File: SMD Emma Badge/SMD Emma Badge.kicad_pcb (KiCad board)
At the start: 2 copper layers, 1 part, among them J1 Conn_01x02_Male

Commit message: Working through basics of the LFSR
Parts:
- added C201: 10u, Capacitor_SMD:C_0603_1608Metric, F.Cu at (146.1, 80.0)
- added C202: 8.2n, Capacitor_SMD:C_0603_1608Metric, F.Cu at (158.8, 78.7)
- added C203: 0.1uF, Capacitor_SMD:C_0603_1608Metric, F.Cu at (157.5, 71.1)
- added C301: 10u, Capacitor_SMD:C_0603_1608Metric, F.Cu at (82.5, 74.9)
- added C302: 8.2n, Capacitor_SMD:C_0603_1608Metric, F.Cu at (96.1, 72.4)
- added C303: 0.1uF, Capacitor_SMD:C_0603_1608Metric, F.Cu at (96.5, 68.6)
- added C401: 0.1uF, Capacitor_SMD:C_0603_1608Metric, F.Cu at (96.5, 88.9)
- added C402: 0.1uF, Capacitor_SMD:C_0603_1608Metric, F.Cu at (97.8, 77.5)
- added C403: 0.1uF, Capacitor_SMD:C_0603_1608Metric, F.Cu at (110.5, 87.6)
- added C404: 0.1uF, Capacitor_SMD:C_0603_1608Metric, F.Cu at (127.0, 87.6)
- added C405: 0.1uF, Capacitor_SMD:C_0603_1608Metric, F.Cu at (113.0, 77.5)
- added R201: 11k, Resistor_SMD:R_0603_1608Metric, F.Cu at (146.1, 72.4)
- added R202: 11k, Resistor_SMD:R_0603_1608Metric, F.Cu at (146.1, 76.2)
- added R203: 1k, Resistor_SMD:R_0603_1608Metric, F.Cu at (162.6, 73.7)
- added R301: 1k, Resistor_SMD:R_0603_1608Metric, F.Cu at (82.5, 67.3)
- added R302: 1k, Resistor_SMD:R_0603_1608Metric, F.Cu at (82.5, 71.1)
- added R303: 1k, Resistor_SMD:R_0603_1608Metric, F.Cu at (101.6, 68.6)
- added U101: AMS1117-5.0, Package_TO_SOT_SMD:SOT-223-3_TabPin2, F.Cu at (127.0, 67.3)
- added U201: LM555xM, Package_SO:SOIC-8_3.9x4.9mm_P1.27mm, F.Cu at (152.8, 76.8)
- added U301: LM555xM, Package_SO:SOIC-8_3.9x4.9mm_P1.27mm, F.Cu at (89.8, 70.7)
- added U401: 74164, Package_SO:SOIC-14_3.9x8.7mm_P1.27mm, F.Cu at (102.9, 92.7)
- added U402: 74LS595, Package_SO:SOIC-16_3.9x9.9mm_P1.27mm, F.Cu at (118.1, 92.7)
- added U403: 74164, Package_SO:SOIC-14_3.9x8.7mm_P1.27mm, F.Cu at (133.3, 92.7)
- added U404: 74HC86, Package_SO:SOIC-14_3.9x8.7mm_P1.27mm, F.Cu at (118.1, 83.8)
- added U405: 74HC04, Package_SO:SOIC-14_3.9x8.7mm_P1.27mm, F.Cu at (102.9, 83.8)
- renumbered J1 to J101
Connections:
- J101 pad 2: Net-(J1-Pad2) -> GND

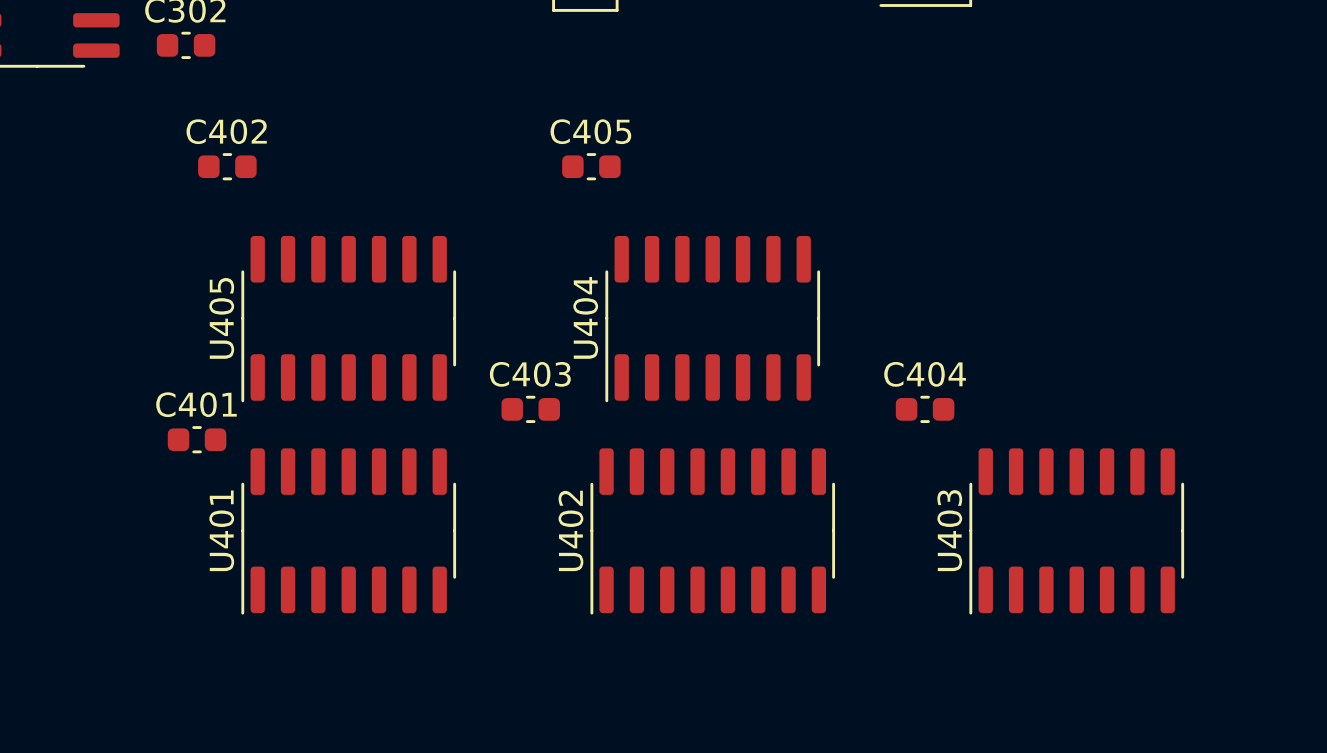
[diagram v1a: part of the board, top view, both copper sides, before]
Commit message: Add power-on reset
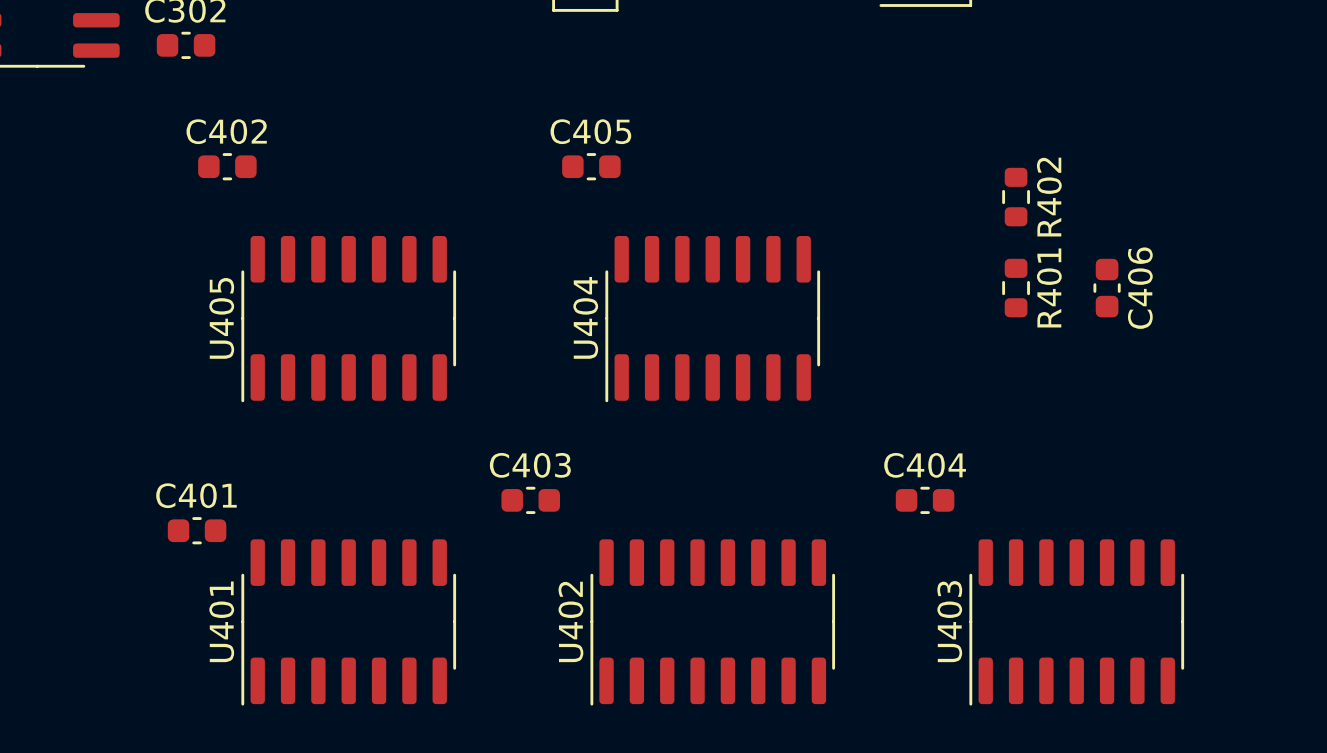
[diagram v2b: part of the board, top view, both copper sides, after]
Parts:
- added C406: 10u, Capacitor_SMD:C_0603_1608Metric, F.Cu at (134.6, 82.5)
- added R401: 180k, Resistor_SMD:R_0603_1608Metric, F.Cu at (130.8, 82.5)
- added R402: 1k, Resistor_SMD:R_0603_1608Metric, F.Cu at (130.8, 78.7)
- moved C403 3.81 mm to (110.5, 91.4)
- moved C404 3.81 mm to (127.0, 91.4)
- moved U401 3.81 mm to (102.9, 96.5)
- moved U402 3.81 mm to (118.1, 96.5)
- moved U403 3.81 mm to (133.3, 96.5)
- moved C401 3.81 mm to (96.5, 92.7)

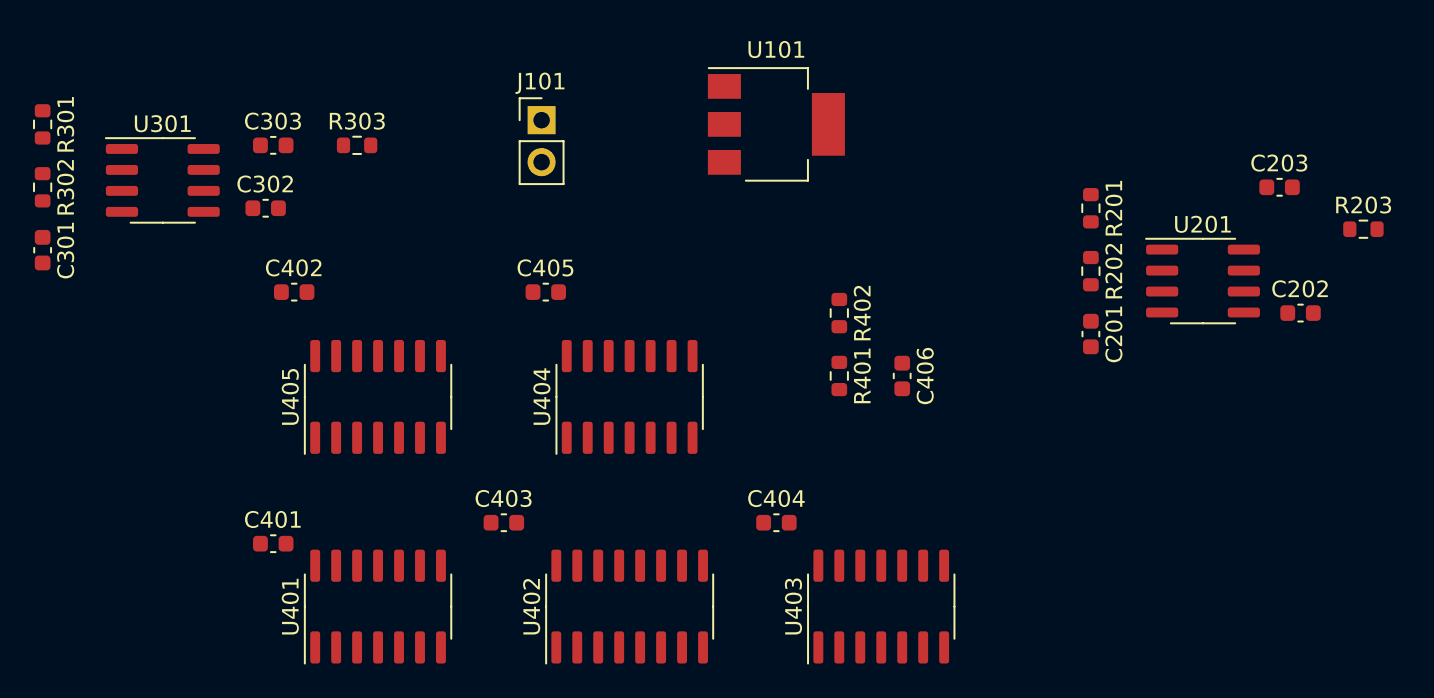
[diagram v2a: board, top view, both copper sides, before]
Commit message: Routing the registers
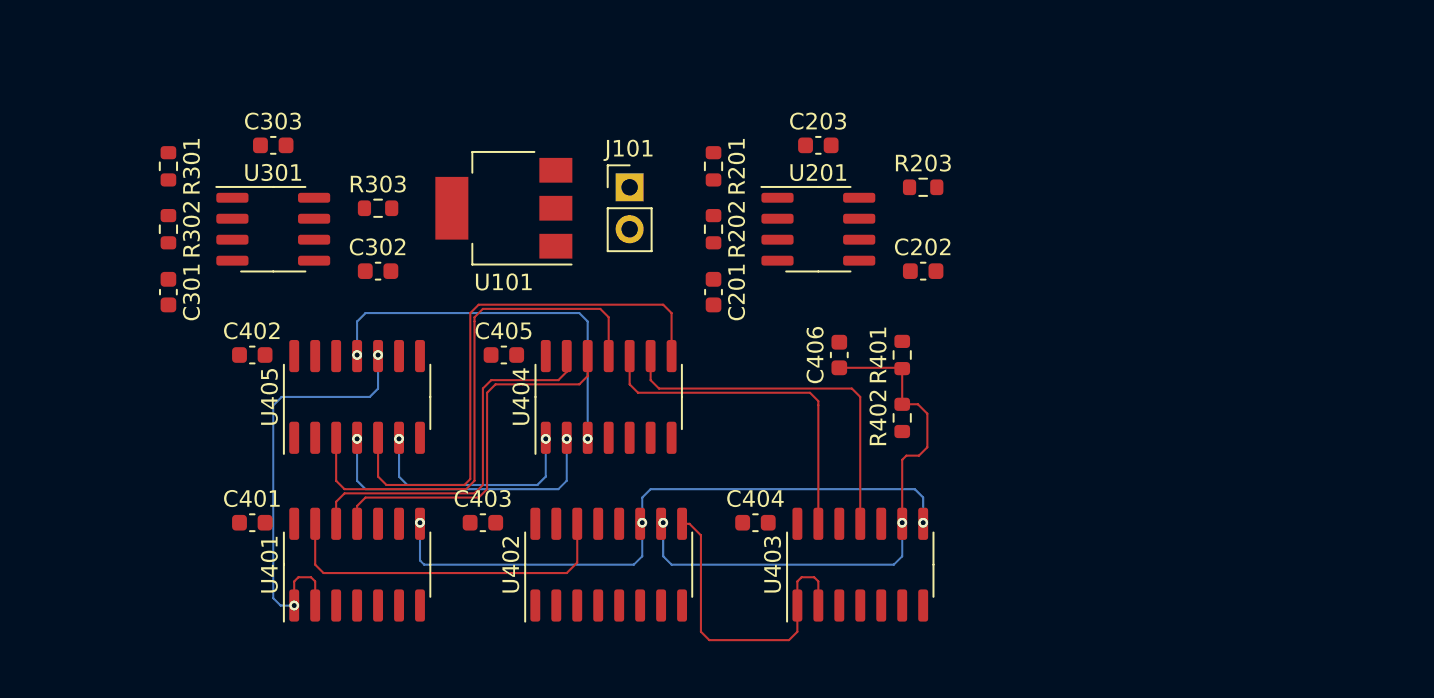
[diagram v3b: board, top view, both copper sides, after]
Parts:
- moved C203 28.1 mm to (129.5, 68.6)
- moved R203 26.8 mm to (135.9, 71.1)
- moved U201 23.5 mm to (129.5, 73.7)
- moved C201 23.0 mm to (123.2, 77.5)
- moved C202 23.0 mm to (135.9, 76.2)
- moved R201 23.0 mm to (123.2, 69.8)
- moved R202 23.0 mm to (123.2, 73.7)
- moved U101 17.3 mm to (110.5, 72.4), turned to 180 degrees
- moved C301 8.03 mm to (90.2, 77.5)
- moved R301 8.03 mm to (90.2, 69.8)
- moved R302 8.03 mm to (90.2, 73.7)
- moved C302 7.80 mm to (102.9, 76.2)
- moved R402 7.41 mm to (134.6, 85.1), turned to 90 degrees
- moved U301 7.31 mm to (96.5, 73.7)
- moved J101 6.71 mm to (118.1, 71.1)
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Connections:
- C203 pad 1: +5V -> GND
- C203 pad 2: GND -> +5V
- C303 pad 1: +5V -> GND
- C303 pad 2: GND -> +5V
- C401 pad 1: +5V -> GND
- C401 pad 2: GND -> +5V
- C404 pad 1: +5V -> GND
- C404 pad 2: GND -> +5V
- U404 pad 1: /LFSR/TAP6 -> Net-(U404-Pad1)
- U404 pad 10: Net-(U404-Pad10) -> /LFSR/TAP24
- U404 pad 12: GND -> /LFSR/TAP6
- U404 pad 13: GND -> /LFSR/TAP7
- U404 pad 2: /LFSR/TAP7 -> Net-(U404-Pad2)
- U404 pad 4: /LFSR/TAP22 -> GND
- U404 pad 5: /LFSR/TAP24 -> GND
- U404 pad 9: Net-(U404-Pad9) -> /LFSR/TAP22
- U405 pad 1: Net-(U404-Pad3) -> GND
- U405 pad 10: Net-(U405-Pad10) -> /LFSR/INPUT
- U405 pad 11: GND -> Net-(U404-Pad3)
- U405 pad 2: Net-(U404-Pad9) -> Net-(U405-Pad2)
- U405 pad 3: Net-(U404-Pad6) -> Net-(U404-Pad11)
- U405 pad 4: Net-(U404-Pad10) -> Net-(U404-Pad2)
- U405 pad 6: /LFSR/INPUT -> Net-(U404-Pad1)
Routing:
- net /Register Clock/CLK: track 0.00 -> 38.6 mm, vias 0 -> 3
- net /LFSR/PWRCLR: track 0.00 -> 34.5 mm, vias 0 -> 2
- net Net-(U404-Pad8): track 0.00 -> 33.6 mm
- net Net-(U404-Pad11): track 0.00 -> 32.2 mm
- net /LFSR/INPUT: track 0.00 -> 26.3 mm, vias 0 -> 2
- net Net-(U404-Pad3): track 0.00 -> 23.5 mm, vias 0 -> 2
- net /LFSR/TAP7: track 0.00 -> 22.9 mm
- net /LFSR/TAP6: track 0.00 -> 22.9 mm
- net /LFSR/TAP22: track 0.00 -> 22.3 mm
- net Net-(U401-Pad13): track 0.00 -> 21.2 mm
- net /LFSR/TAP24: track 0.00 -> 21.0 mm
- net Net-(U402-Pad9): track 0.00 -> 19.5 mm
- net Net-(U404-Pad2): track 0.00 -> 18.2 mm, vias 0 -> 2
- net Net-(U404-Pad1): track 0.00 -> 13.9 mm, vias 0 -> 2

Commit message: Working on letters
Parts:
- added D501: LED, LED_SMD:LED_0603_1608Metric, F.Cu at (69.8, 108.0)
- added D502: LED, LED_SMD:LED_0603_1608Metric, F.Cu at (73.7, 108.0)
- added D503: LED, LED_SMD:LED_0603_1608Metric, F.Cu at (77.5, 108.0)
- added D504: LED, LED_SMD:LED_0603_1608Metric, F.Cu at (81.3, 108.0)
- added D505: LED, LED_SMD:LED_0603_1608Metric, F.Cu at (85.1, 108.0)
- added D506: LED, LED_SMD:LED_0603_1608Metric, F.Cu at (69.8, 111.5)
- added D507: LED, LED_SMD:LED_0603_1608Metric, F.Cu at (69.8, 115.1)
- added D508: LED, LED_SMD:LED_0603_1608Metric, F.Cu at (69.8, 118.6)
- added D509: LED, LED_SMD:LED_0603_1608Metric, F.Cu at (73.7, 118.6)
- added D510: LED, LED_SMD:LED_0603_1608Metric, F.Cu at (77.5, 118.6)
- added D511: LED, LED_SMD:LED_0603_1608Metric, F.Cu at (81.3, 118.6)
- added D512: LED, LED_SMD:LED_0603_1608Metric, F.Cu at (69.8, 122.2)
- added D513: LED, LED_SMD:LED_0603_1608Metric, F.Cu at (69.8, 125.7)
- added D514: LED, LED_SMD:LED_0603_1608Metric, F.Cu at (69.8, 129.3)
- added D515: LED, LED_SMD:LED_0603_1608Metric, F.Cu at (73.7, 129.3)
- added D516: LED, LED_SMD:LED_0603_1608Metric, F.Cu at (77.5, 129.3)
- added D517: LED, LED_SMD:LED_0603_1608Metric, F.Cu at (81.3, 129.3)
- added D518: LED, LED_SMD:LED_0603_1608Metric, F.Cu at (85.1, 129.3)
- added D601: LED, LED_SMD:LED_0603_1608Metric, F.Cu at (91.4, 108.0)
- added D602: LED, LED_SMD:LED_0603_1608Metric, F.Cu at (106.7, 108.0)
- added D603: LED, LED_SMD:LED_0603_1608Metric, F.Cu at (91.4, 111.5)
- added D604: LED, LED_SMD:LED_0603_1608Metric, F.Cu at (95.2, 111.5)
- added D605: LED, LED_SMD:LED_0603_1608Metric, F.Cu at (102.9, 111.5)
- added D606: LED, LED_SMD:LED_0603_1608Metric, F.Cu at (106.7, 111.5)
- added D607: LED, LED_SMD:LED_0603_1608Metric, F.Cu at (91.4, 115.1)
- added D608: LED, LED_SMD:LED_0603_1608Metric, F.Cu at (99.1, 115.1)
- added D609: LED, LED_SMD:LED_0603_1608Metric, F.Cu at (106.7, 115.1)
- added D610: LED, LED_SMD:LED_0603_1608Metric, F.Cu at (91.4, 118.6)
- added D611: LED, LED_SMD:LED_0603_1608Metric, F.Cu at (99.1, 118.6)
- added D612: LED, LED_SMD:LED_0603_1608Metric, F.Cu at (106.7, 118.6)
- added D613: LED, LED_SMD:LED_0603_1608Metric, F.Cu at (91.4, 122.2)
- added D614: LED, LED_SMD:LED_0603_1608Metric, F.Cu at (106.7, 122.2)
- added D615: LED, LED_SMD:LED_0603_1608Metric, F.Cu at (91.4, 125.7)
- added D616: LED, LED_SMD:LED_0603_1608Metric, F.Cu at (106.7, 125.7)
- added D617: LED, LED_SMD:LED_0603_1608Metric, F.Cu at (91.4, 129.3)
- added D618: LED, LED_SMD:LED_0603_1608Metric, F.Cu at (106.7, 129.3)
- added D701: LED, LED_SMD:LED_0603_1608Metric, F.Cu at (113.0, 108.0)
- added D702: LED, LED_SMD:LED_0603_1608Metric, F.Cu at (128.3, 108.0)
- added D703: LED, LED_SMD:LED_0603_1608Metric, F.Cu at (113.0, 111.5)
- added D704: LED, LED_SMD:LED_0603_1608Metric, F.Cu at (116.8, 111.5)
- added D705: LED, LED_SMD:LED_0603_1608Metric, F.Cu at (124.5, 111.5)
- added D706: LED, LED_SMD:LED_0603_1608Metric, F.Cu at (128.3, 111.5)
- added D707: LED, LED_SMD:LED_0603_1608Metric, F.Cu at (113.0, 115.1)
- added D708: LED, LED_SMD:LED_0603_1608Metric, F.Cu at (120.7, 115.1)
- added D709: LED, LED_SMD:LED_0603_1608Metric, F.Cu at (128.3, 115.1)
- added D710: LED, LED_SMD:LED_0603_1608Metric, F.Cu at (113.0, 118.6)
- added D711: LED, LED_SMD:LED_0603_1608Metric, F.Cu at (120.7, 118.6)
- added D712: LED, LED_SMD:LED_0603_1608Metric, F.Cu at (128.3, 118.6)
- added D713: LED, LED_SMD:LED_0603_1608Metric, F.Cu at (113.0, 122.2)
- added D714: LED, LED_SMD:LED_0603_1608Metric, F.Cu at (128.3, 122.2)
- added D715: LED, LED_SMD:LED_0603_1608Metric, F.Cu at (113.0, 125.7)
- added D716: LED, LED_SMD:LED_0603_1608Metric, F.Cu at (128.3, 125.7)
- added D717: LED, LED_SMD:LED_0603_1608Metric, F.Cu at (113.0, 129.3)
- added D718: LED, LED_SMD:LED_0603_1608Metric, F.Cu at (128.3, 129.3)
- added D801: LED, LED_SMD:LED_0603_1608Metric, F.Cu at (142.2, 108.0)
- added D802: LED, LED_SMD:LED_0603_1608Metric, F.Cu at (138.4, 111.5)
- added D803: LED, LED_SMD:LED_0603_1608Metric, F.Cu at (146.1, 111.5)
- added D804: LED, LED_SMD:LED_0603_1608Metric, F.Cu at (134.6, 115.1)
- added D805: LED, LED_SMD:LED_0603_1608Metric, F.Cu at (149.9, 115.1)
- added D806: LED, LED_SMD:LED_0603_1608Metric, F.Cu at (134.6, 118.6)
- added D807: LED, LED_SMD:LED_0603_1608Metric, F.Cu at (149.9, 118.6)
- added D808: LED, LED_SMD:LED_0603_1608Metric, F.Cu at (134.6, 122.2)
- added D809: LED, LED_SMD:LED_0603_1608Metric, F.Cu at (138.4, 122.2)
- added D810: LED, LED_SMD:LED_0603_1608Metric, F.Cu at (142.2, 122.2)
- added D811: LED, LED_SMD:LED_0603_1608Metric, F.Cu at (146.1, 122.2)
- added D812: LED, LED_SMD:LED_0603_1608Metric, F.Cu at (149.9, 122.2)
- added D813: LED, LED_SMD:LED_0603_1608Metric, F.Cu at (134.6, 125.7)
- added D814: LED, LED_SMD:LED_0603_1608Metric, F.Cu at (149.9, 125.7)
- added D815: LED, LED_SMD:LED_0603_1608Metric, F.Cu at (134.6, 129.3)
- added D816: LED, LED_SMD:LED_0603_1608Metric, F.Cu at (149.9, 129.3)
- added H101: MountingHole, MountingHole:MountingHole_2.5mm, F.Cu at (71.1, 77.5)
- added H102: MountingHole, MountingHole:MountingHole_2.5mm, F.Cu at (148.6, 77.5)
- added Q501: MMBT3904, Package_TO_SOT_SMD:SOT-23, F.Cu at (77.5, 105.4)
- added Q601: MMBT3904, Package_TO_SOT_SMD:SOT-23, F.Cu at (99.1, 105.4)
- added Q701: MMBT3904, Package_TO_SOT_SMD:SOT-23, F.Cu at (120.7, 105.4)
- added Q801: MMBT3904, Package_TO_SOT_SMD:SOT-23, F.Cu at (142.2, 105.4)
- added R501: 1k, Resistor_SMD:R_0603_1608Metric, F.Cu at (69.8, 109.7)
- added R502: 1k, Resistor_SMD:R_0603_1608Metric, F.Cu at (73.7, 109.7)
- added R503: 1k, Resistor_SMD:R_0603_1608Metric, F.Cu at (77.5, 109.7)
- added R504: 1k, Resistor_SMD:R_0603_1608Metric, F.Cu at (81.3, 109.7)
- added R505: 1k, Resistor_SMD:R_0603_1608Metric, F.Cu at (85.1, 109.7)
- added R506: 1k, Resistor_SMD:R_0603_1608Metric, F.Cu at (69.8, 113.3)
- added R507: 1k, Resistor_SMD:R_0603_1608Metric, F.Cu at (69.8, 116.8)
- added R508: 1k, Resistor_SMD:R_0603_1608Metric, F.Cu at (69.8, 120.4)
- added R509: 1k, Resistor_SMD:R_0603_1608Metric, F.Cu at (73.7, 120.4)
- added R510: 1k, Resistor_SMD:R_0603_1608Metric, F.Cu at (77.5, 120.4)
- added R511: 1k, Resistor_SMD:R_0603_1608Metric, F.Cu at (81.3, 120.4)
- added R512: 1k, Resistor_SMD:R_0603_1608Metric, F.Cu at (69.8, 124.0)
- added R513: 1k, Resistor_SMD:R_0603_1608Metric, F.Cu at (69.8, 127.5)
- added R514: 1k, Resistor_SMD:R_0603_1608Metric, F.Cu at (69.8, 131.1)
- added R515: 1k, Resistor_SMD:R_0603_1608Metric, F.Cu at (73.7, 131.1)
- added R516: 1k, Resistor_SMD:R_0603_1608Metric, F.Cu at (77.5, 131.1)
- added R517: 1k, Resistor_SMD:R_0603_1608Metric, F.Cu at (81.3, 131.1)
- added R518: 1k, Resistor_SMD:R_0603_1608Metric, F.Cu at (85.1, 131.1)
- added R519: 11k, Resistor_SMD:R_0603_1608Metric, F.Cu at (78.7, 101.6)
- added R601: 1k, Resistor_SMD:R_0603_1608Metric, F.Cu at (91.4, 109.7)
- added R602: 1k, Resistor_SMD:R_0603_1608Metric, F.Cu at (106.7, 109.7)
- added R603: 1k, Resistor_SMD:R_0603_1608Metric, F.Cu at (91.4, 113.3)
- added R604: 1k, Resistor_SMD:R_0603_1608Metric, F.Cu at (95.2, 113.3)
- added R605: 1k, Resistor_SMD:R_0603_1608Metric, F.Cu at (102.9, 113.3)
- added R606: 1k, Resistor_SMD:R_0603_1608Metric, F.Cu at (106.7, 113.3)
- added R607: 1k, Resistor_SMD:R_0603_1608Metric, F.Cu at (91.4, 116.8)
- added R608: 1k, Resistor_SMD:R_0603_1608Metric, F.Cu at (99.1, 116.8)
- added R609: 1k, Resistor_SMD:R_0603_1608Metric, F.Cu at (106.7, 116.8)
- added R610: 1k, Resistor_SMD:R_0603_1608Metric, F.Cu at (91.4, 120.4)
- added R611: 1k, Resistor_SMD:R_0603_1608Metric, F.Cu at (99.1, 120.4)
- added R612: 1k, Resistor_SMD:R_0603_1608Metric, F.Cu at (106.7, 120.4)
- added R613: 1k, Resistor_SMD:R_0603_1608Metric, F.Cu at (91.4, 124.0)
- added R614: 1k, Resistor_SMD:R_0603_1608Metric, F.Cu at (106.7, 124.0)
- added R615: 1k, Resistor_SMD:R_0603_1608Metric, F.Cu at (91.4, 127.5)
- added R616: 1k, Resistor_SMD:R_0603_1608Metric, F.Cu at (106.7, 127.5)
- added R617: 1k, Resistor_SMD:R_0603_1608Metric, F.Cu at (91.4, 131.1)
- added R618: 1k, Resistor_SMD:R_0603_1608Metric, F.Cu at (106.7, 131.1)
- added R619: 11k, Resistor_SMD:R_0603_1608Metric, F.Cu at (100.3, 101.6)
- added R701: 1k, Resistor_SMD:R_0603_1608Metric, F.Cu at (113.0, 109.7)
- added R702: 1k, Resistor_SMD:R_0603_1608Metric, F.Cu at (128.3, 109.7)
- added R703: 1k, Resistor_SMD:R_0603_1608Metric, F.Cu at (113.0, 113.3)
- added R704: 1k, Resistor_SMD:R_0603_1608Metric, F.Cu at (116.8, 113.3)
- added R705: 1k, Resistor_SMD:R_0603_1608Metric, F.Cu at (124.5, 113.3)
- added R706: 1k, Resistor_SMD:R_0603_1608Metric, F.Cu at (128.3, 113.3)
- added R707: 1k, Resistor_SMD:R_0603_1608Metric, F.Cu at (113.0, 116.8)
- added R708: 1k, Resistor_SMD:R_0603_1608Metric, F.Cu at (120.7, 116.8)
- added R709: 1k, Resistor_SMD:R_0603_1608Metric, F.Cu at (128.3, 116.8)
- added R710: 1k, Resistor_SMD:R_0603_1608Metric, F.Cu at (113.0, 120.4)
- added R711: 1k, Resistor_SMD:R_0603_1608Metric, F.Cu at (120.7, 120.4)
- added R712: 1k, Resistor_SMD:R_0603_1608Metric, F.Cu at (128.3, 120.4)
- added R713: 1k, Resistor_SMD:R_0603_1608Metric, F.Cu at (113.0, 124.0)
- added R714: 1k, Resistor_SMD:R_0603_1608Metric, F.Cu at (128.3, 124.0)
- added R715: 1k, Resistor_SMD:R_0603_1608Metric, F.Cu at (113.0, 127.5)
- added R716: 1k, Resistor_SMD:R_0603_1608Metric, F.Cu at (128.3, 127.5)
- added R717: 1k, Resistor_SMD:R_0603_1608Metric, F.Cu at (113.0, 131.1)
- added R718: 1k, Resistor_SMD:R_0603_1608Metric, F.Cu at (128.3, 131.1)
- added R719: 11k, Resistor_SMD:R_0603_1608Metric, F.Cu at (121.9, 101.6)
- added R801: 1k, Resistor_SMD:R_0603_1608Metric, F.Cu at (142.2, 109.7)
- added R802: 1k, Resistor_SMD:R_0603_1608Metric, F.Cu at (138.4, 113.3)
- added R803: 1k, Resistor_SMD:R_0603_1608Metric, F.Cu at (146.1, 113.3)
- added R804: 1k, Resistor_SMD:R_0603_1608Metric, F.Cu at (134.6, 116.8)
- added R805: 1k, Resistor_SMD:R_0603_1608Metric, F.Cu at (149.9, 116.8)
- added R806: 1k, Resistor_SMD:R_0603_1608Metric, F.Cu at (134.6, 120.4)
- added R807: 1k, Resistor_SMD:R_0603_1608Metric, F.Cu at (149.9, 120.4)
- added R808: 1k, Resistor_SMD:R_0603_1608Metric, F.Cu at (134.6, 124.0)
- added R809: 1k, Resistor_SMD:R_0603_1608Metric, F.Cu at (138.4, 124.0)
- added R810: 1k, Resistor_SMD:R_0603_1608Metric, F.Cu at (142.2, 124.0)
- added R811: 1k, Resistor_SMD:R_0603_1608Metric, F.Cu at (146.1, 124.0)
- added R812: 1k, Resistor_SMD:R_0603_1608Metric, F.Cu at (149.9, 124.0)
- added R813: 1k, Resistor_SMD:R_0603_1608Metric, F.Cu at (134.6, 127.5)
- added R814: 1k, Resistor_SMD:R_0603_1608Metric, F.Cu at (149.9, 127.5)
- added R815: 1k, Resistor_SMD:R_0603_1608Metric, F.Cu at (134.6, 131.1)
- added R816: 1k, Resistor_SMD:R_0603_1608Metric, F.Cu at (149.9, 131.1)
- added R819: 11k, Resistor_SMD:R_0603_1608Metric, F.Cu at (143.5, 101.6)
- moved J101 46.2 mm to (73.7, 83.8), turned to 90 degrees
- moved U101 40.0 mm to (74.9, 90.8), turned to 270 degrees
- moved C202 31.0 mm to (148.6, 95.2), turned to 0 degrees
- moved R202 31.0 mm to (141.0, 95.2), turned to 0 degrees
- moved R203 30.5 mm to (144.8, 95.2), turned to 0 degrees
- moved R302 26.2 mm to (83.8, 95.2), turned to 0 degrees
- moved C301 24.7 mm to (82.5, 88.9), turned to 90 degrees
- moved C201 22.7 mm to (139.7, 88.9), turned to 90 degrees
- moved R303 21.7 mm to (87.6, 95.2), turned to 0 degrees
- moved U201 21.6 mm to (144.8, 88.9), turned to 90 degrees
- moved R301 19.4 mm to (86.4, 82.5), turned to 90 degrees
- moved C302 17.8 mm to (91.4, 95.2), turned to 0 degrees
- moved U301 17.6 mm to (87.6, 88.9), turned to 90 degrees
- moved C303 14.2 mm to (90.2, 82.5), turned to 90 degrees
- moved R201 13.1 mm to (142.2, 82.5), turned to 90 degrees
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- renumbered C203 to C201, C201 to C202, C202 to C203, C303 to C301, C301 to C302, C302 to C303, C403 to C401, C406 to C402, C401 to C403, C402 to C406, R203 to R201, R201 to R202, R202 to R203, R303 to R301, R301 to R302, R302 to R303, R402 to R401, R401 to R402, U405 to U404, U404 to U405
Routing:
- net /LFSR/DISPE: track 0.00 -> 38.6 mm
- net /LFSR/DISPA: track 0.00 -> 29.8 mm
- net /LFSR/DISPM1: track 0.00 -> 18.3 mm
- net /LFSR/DISPM2: track 0.00 -> 9.37 mm
- net Net-(J101-Pad1): track 0.00 -> 4.24 mm
- net Net-(Q701-Pad1): track 0.00 -> 2.12 mm
- net Net-(Q801-Pad1): track 0.00 -> 2.12 mm
- net Net-(Q601-Pad1): track 0.00 -> 2.12 mm
- net Net-(Q501-Pad1): track 0.00 -> 2.12 mm
- net Net-(D802-Pad1): track 0.00 -> 1.79 mm
- net Net-(D806-Pad1): track 0.00 -> 1.79 mm
- net Net-(D804-Pad1): track 0.00 -> 1.79 mm
- net Net-(D706-Pad1): track 0.00 -> 1.79 mm
- net Net-(D703-Pad1): track 0.00 -> 1.79 mm
- net Net-(D604-Pad1): track 0.00 -> 1.79 mm
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- added copper zone on F.Cu, net /LED-A/COLL
- added copper zone on F.Cu, net /LED-E/COLL
- added copper zone on F.Cu, net /LED-M1/COLL
- added copper zone on F.Cu, net /LED-M2/COLL
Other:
- board outline added: 87.6 x 63.5 mm
- board text added: "+9V"
- board text added: "GND"
